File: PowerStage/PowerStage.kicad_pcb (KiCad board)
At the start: 2 copper layers, 28.8 x 16.3 mm, 19 parts, among them IC1 ATtiny404-SS, IC2 MAX40200AUK, IC3 74LVC1G07GC, IC4 74LVC1G07GC, K1 Conn_01x02, K2 Conn_01x05, K3 DBG/UPDI, Q1 Q_PMOS_GSD

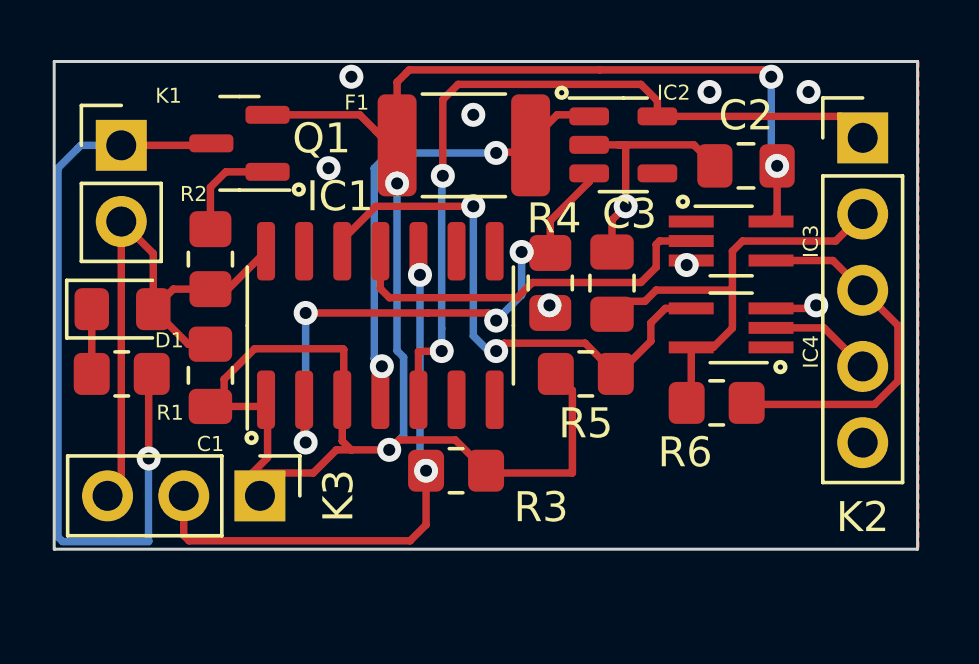
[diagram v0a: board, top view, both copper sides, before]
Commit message: Fixes in the schematic
Some fixes in the schematic
Not routed
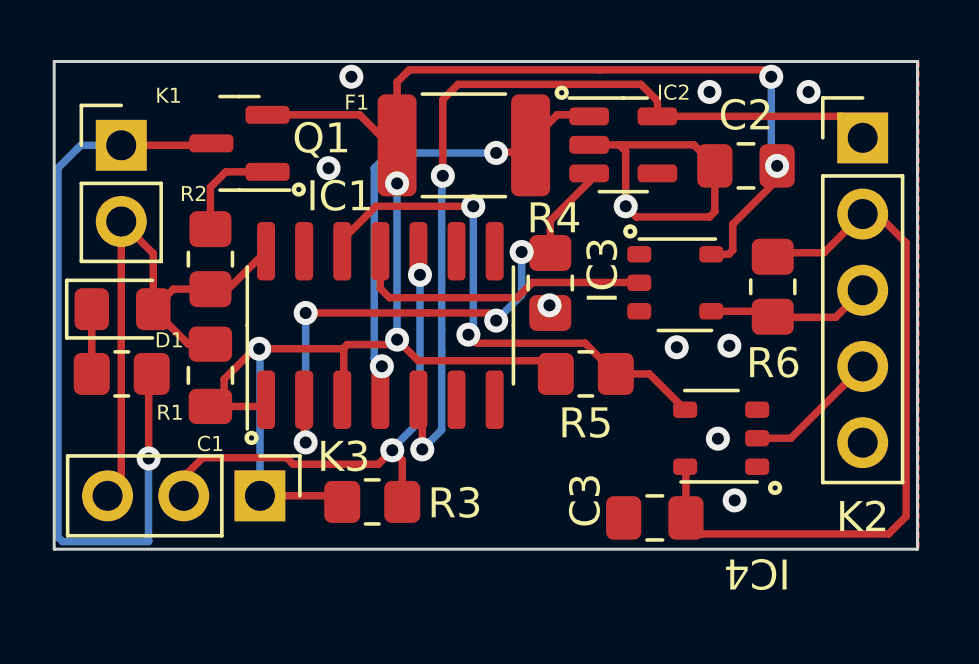
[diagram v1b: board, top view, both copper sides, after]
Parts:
- IC3, IC4: footprint Package_TO_SOT_SMD:SOT-353_SC-70-5_Handsoldering -> SC-74A_SOT753:SC-74A
- moved C3 7.96 mm to (125.7, 86.3), turned to 180 degrees
- moved IC4 4.71 mm to (129.1, 84.6)
- moved R6 4.30 mm to (129.6, 78.6), turned to -90 degrees
- moved IC3 3.10 mm to (125.2, 77.5)
- moved R3 2.98 mm to (116.3, 85.8), turned to 0 degrees
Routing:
- net VIN_3V3: track 15.2 -> 23.8 mm
- net TX: track 12.5 -> 5.22 mm
- net BAT_IN: track 65.4 -> 58.7 mm, vias 4 -> 5
- net VOUT: track 26.0 -> 28.9 mm
- net PA1: track 13.0 -> 10.2 mm
- net UPDI: track 18.1 -> 16.2 mm
- net GND: track 29.9 -> 31.0 mm, vias 9 -> 10
- net PA2: track 18.8 -> 17.8 mm
- net RX: track 3.59 -> 4.51 mm

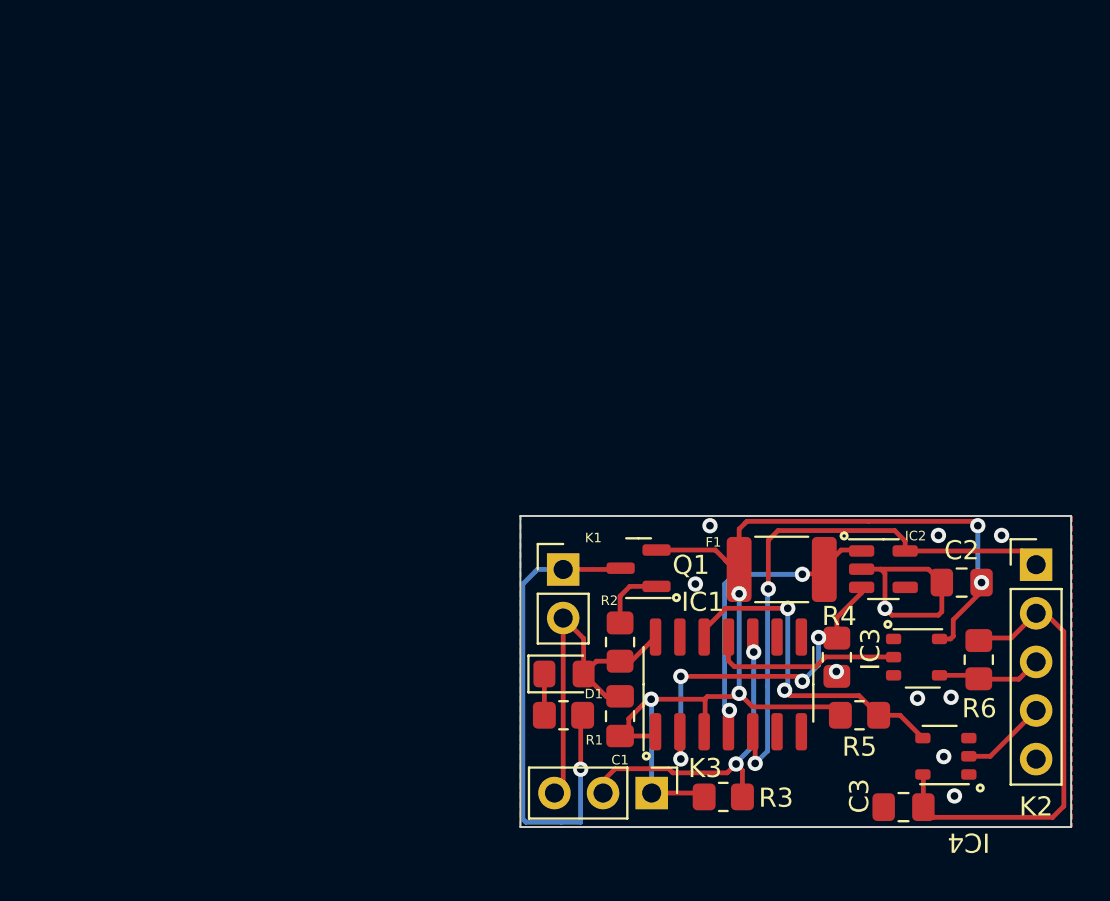
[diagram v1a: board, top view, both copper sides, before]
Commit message: Updated PCB
PCB and Schamtic has been updated
Not neeed connections removed
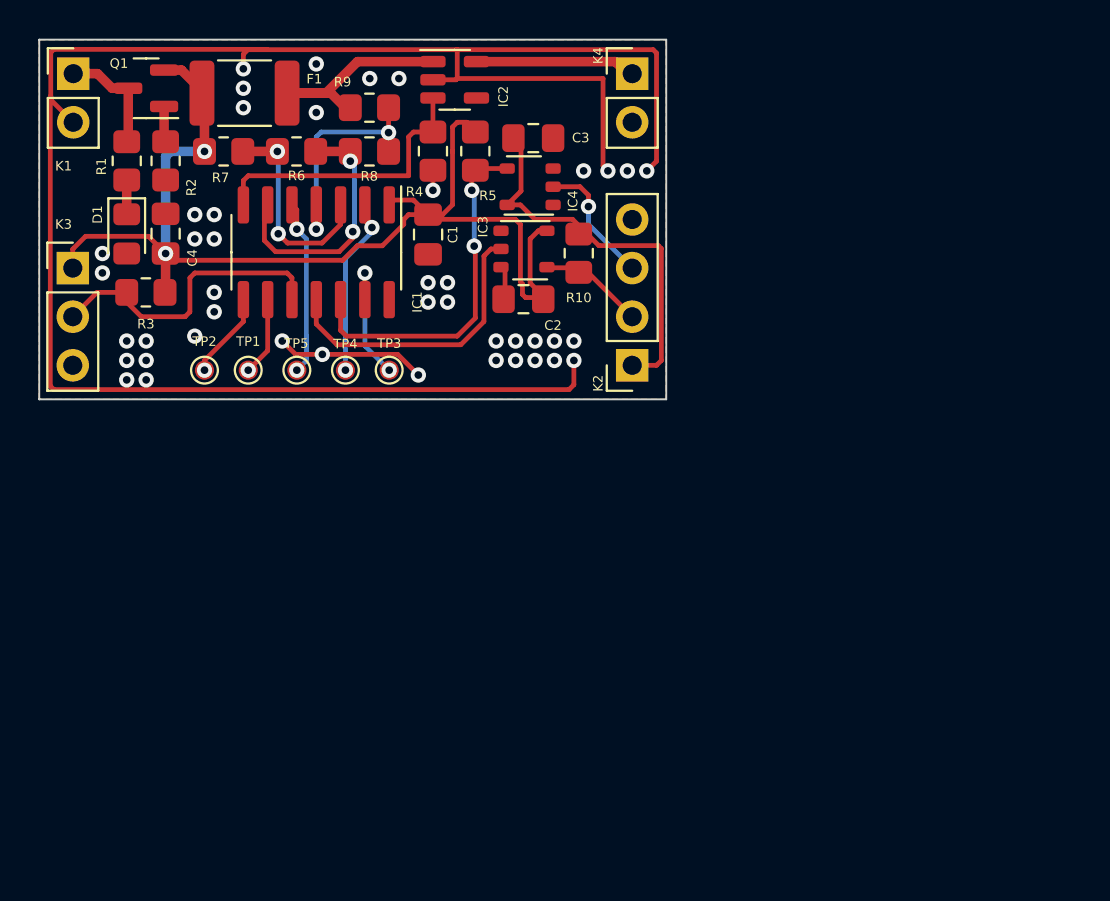
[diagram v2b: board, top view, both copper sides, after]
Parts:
- added C4: 10uF/10V, Capacitor_SMD:C_0805_2012Metric_Pad1.18x1.45mm_HandSolder, F.Cu at (87.1, 56.4)
- added K4: Conn_01x02, Connector_PinHeader_2.54mm:PinHeader_1x02_P2.54mm_Vertical, F.Cu at (111.5, 48.0)
- added R10: 10k, Resistor_SMD:R_0805_2012Metric_Pad1.20x1.40mm_HandSolder, F.Cu at (108.7, 57.4)
- added R7: 10k, Resistor_SMD:R_0805_2012Metric_Pad1.20x1.40mm_HandSolder, F.Cu at (90.2, 52.1)
- added R8: 10k, Resistor_SMD:R_0805_2012Metric_Pad1.20x1.40mm_HandSolder, F.Cu at (97.8, 52.1)
- added R9: 10k, Resistor_SMD:R_0805_2012Metric_Pad1.20x1.40mm_HandSolder, F.Cu at (97.8, 49.8)
- added TP1: PB0, TestPoint:TestPoint_Pad_D1.0mm, F.Cu at (91.4, 63.5)
- added TP2: PB1, TestPoint:TestPoint_Pad_D1.0mm, F.Cu at (89.2, 63.5)
- added TP3: PA3, TestPoint:TestPoint_Pad_D1.0mm, F.Cu at (98.8, 63.5)
- added TP4: PA4, TestPoint:TestPoint_Pad_D1.0mm, F.Cu at (96.5, 63.5)
- added TP5: PA7, TestPoint:TestPoint_Pad_D1.0mm, F.Cu at (94.0, 63.5)
- K2: value Conn_01x05 -> Conn_01x04; footprint Connector_PinHeader_2.54mm:PinHeader_1x05_P2.54mm_Vertical -> Connector_PinSocket_2.54mm:PinSocket_1x04_P2.54mm_Vertical
- moved R6 44.5 mm to (94.0, 52.1), turned to 180 degrees
- moved K3 40.8 mm to (82.3, 58.2), turned to 0 degrees
- moved R3 40.1 mm to (86.1, 59.4), turned to 180 degrees
- moved C3 40.0 mm to (106.3, 51.4), turned to 0 degrees
- moved F1 37.5 mm to (91.2, 49.0)
- moved R1 36.9 mm to (85.1, 52.6), turned to -90 degrees
- moved IC4 36.8 mm to (107.4, 54.9)
- moved K1 36.4 mm to (82.3, 48.0)
- moved Q1 35.9 mm to (86.1, 48.8)
- moved R5 35.7 mm to (103.3, 52.1), turned to 90 degrees
- moved R2 34.6 mm to (87.1, 52.6)
- moved IC2 34.0 mm to (102.2, 48.3)
- moved R4 33.8 mm to (101.1, 52.1)
- moved D1 32.4 mm to (85.1, 56.4), turned to -90 degrees
- moved IC1 31.2 mm to (95.0, 57.3), turned to -90 degrees
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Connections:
- net Net-(K1-Pad1) renamed VIN
- IC1 pad 13: unconnected-(IC1-Pad13) -> Net-(IC1-Pad13)
- IC1 pad 3: BAT_IN -> Net-(IC1-Pad3)
- IC1 pad 4: Net-(F1-Pad2) -> Net-(IC1-Pad4)
- IC1 pad 5: VOUT -> Net-(IC1-Pad5)
- IC1 pad 6: unconnected-(IC1-Pad6) -> PB3
- IC1 pad 7: unconnected-(IC1-Pad7) -> PB2
- IC1 pad 8: unconnected-(IC1-Pad8) -> Net-(IC1-Pad8)
- IC1 pad 9: unconnected-(IC1-Pad9) -> Net-(IC1-Pad9)
- IC2 pad 3: Net-(IC1-Pad2) -> PB2
- K2 pad 1: VOUT -> VIN_3V3
- K2 pad 2: VIN_3V3 -> TX
- K2 pad 3: TX -> RX
- K2 pad 4: RX -> GND
- R4 pad 1: Net-(IC1-Pad2) -> PB2
- R6 pad 1: VIN_3V3 -> PB3
- R6 pad 2: TX -> Net-(IC1-Pad3)
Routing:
- net GND: track 31.0 -> 114.2 mm, vias 10 -> 44
- net VIN: track 26.7 -> 6.01 mm, vias 1 -> 0
- net VOUT: track 28.9 -> 8.40 mm, vias 2 -> 0
- net PB2: track 0.00 -> 15.2 mm
- net PB3: track 0.00 -> 13.5 mm, vias 0 -> 2
- net Net-(IC1-Pad4): track 0.00 -> 12.3 mm, vias 0 -> 2
- net Net-(IC1-Pad3): track 0.00 -> 12.0 mm, vias 0 -> 2
- net Net-(IC1-Pad2): track 19.0 -> 9.45 mm, vias 4 -> 2
- net Net-(IC1-Pad5): track 0.00 -> 9.16 mm, vias 0 -> 2
- net Net-(IC1-Pad13): track 0.00 -> 7.00 mm, vias 0 -> 2
- net PA1: track 10.2 -> 15.7 mm
- net Net-(IC1-Pad8): track 0.00 -> 4.53 mm, vias 0 -> 1
- net Net-(F1-Pad2): track 16.0 -> 11.8 mm, vias 2 -> 0
- net Net-(IC1-Pad9): track 0.00 -> 4.11 mm, vias 0 -> 1
- net VIN_3V3: track 23.8 -> 20.4 mm
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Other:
- board size 28.8 x 16.3 mm -> 32.8 x 18.8 mm
- board text removed: "5.5V to 2.5V Input"
- board text removed: "<-TX"
- board text removed: "GND"
- board text removed: "GND (-)"
- board text removed: "In_3V3"
- board text removed: "Low Power Timer for Raspberry Pi Pico (W)"
- board text removed: "RX->"
- board text removed: "UPDI"
- board text removed: "VBat"
- board text removed: "VBat_In (+)"
- board text removed: "Vout"

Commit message: Files for Rev 2 order
Designe send to Aisler
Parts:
- removed TP1: PB0, TestPoint:TestPoint_Pad_D1.0mm
- removed TP2: PB1, TestPoint:TestPoint_Pad_D1.0mm
- removed TP3: PA3, TestPoint:TestPoint_Pad_D1.0mm
- removed TP4: PA4, TestPoint:TestPoint_Pad_D1.0mm
- removed TP5: PA7, TestPoint:TestPoint_Pad_D1.0mm
- added PA3: PA3, TestPoint:TestPoint_Pad_D1.0mm, F.Cu at (98.8, 63.5)
- added PA4: PA4, TestPoint:TestPoint_Pad_D1.0mm, F.Cu at (96.5, 63.5)
- added PA7: PA7, TestPoint:TestPoint_Pad_D1.0mm, F.Cu at (94.0, 63.5)
- added PB0: PB0, TestPoint:TestPoint_Pad_D1.0mm, F.Cu at (91.4, 63.5)
- added PB1: PB1, TestPoint:TestPoint_Pad_D1.0mm, F.Cu at (89.2, 63.5)
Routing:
- net GND: track 114.2 -> 232.1 mm
- net VIN_3V3: track 20.4 -> 16.6 mm, vias 0 -> 1
- net BAT_IN: track 60.4 -> 61.2 mm
- net RX: track 6.79 -> 6.24 mm, vias 1 -> 0
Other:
- board text added: "->TX"
- board text added: "GND"
- board text added: "Power Down Module for Raspberry Pi Pico(W) UART EDITION Rev: 2.0 Date 29/08/2022 By CalM"
- board text added: "RX<-"
- board text added: "UPDI"
- board text added: "VBat(+)"
- board text added: "VIn(+)"
- board text added: "VOut"
- board text added: "V_ext"
